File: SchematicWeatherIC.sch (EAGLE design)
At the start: 27 parts, among them U1 ESP32-C6FH4, U2 MIC5365-3.3YC5-TR

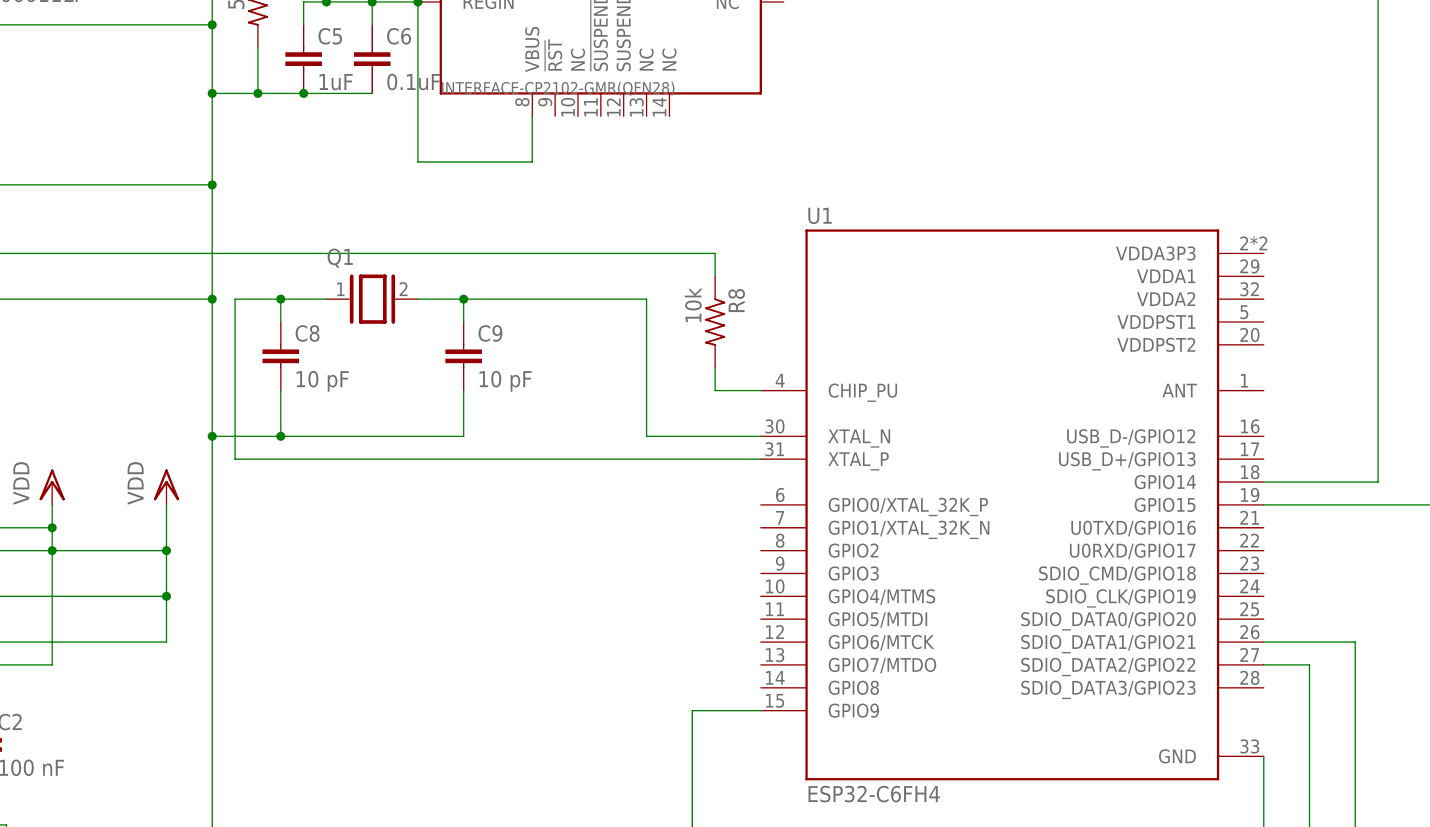
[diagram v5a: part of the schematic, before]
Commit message: connect vdd esp32
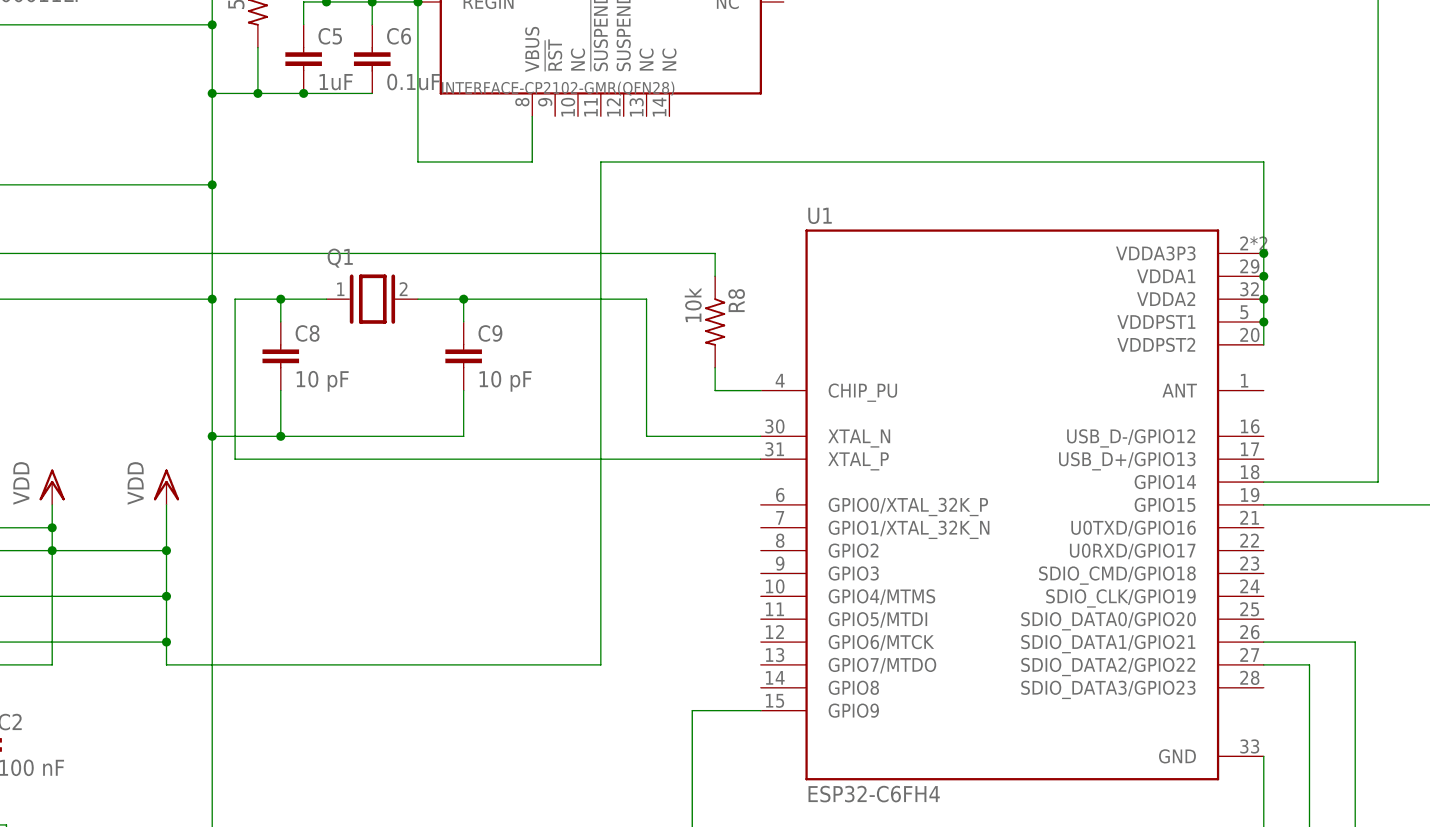
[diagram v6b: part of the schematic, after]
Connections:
- net VDD: now also U1.VDDA1, U1.VDDA2, U1.VDDA3P3, U1.VDDPST1, U1.VDDPST2
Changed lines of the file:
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@@
 <wire x1="58.42" y1="71.12" x2="96.52" y2="71.12" width="0.1524" layer="91"/>
 <junction x="96.52" y="71.12"/>
+<pinref part="U1" gate="G$1" pin="VDDPST2"/>
+<pinref part="U1" gate="G$1" pin="VDDA3P3"/>
+<wire x1="231.14" y1="91.44" x2="231.14" y2="93.98" width="0.1524" layer="91"/>
+<pinref part="U1" gate="G$1" pin="VDDPST1"/>
+<wire x1="231.14" y1="93.98" x2="231.14" y2="96.52" width="0.1524" layer="91"/>
+<junction x="231.14" y="93.98"/>
+<pinref part="U1" gate="G$1" pin="VDDA1"/>
+<wire x1="231.14" y1="96.52" x2="231.14" y2="99.06" width="0.1524" layer="91"/>
+<wire x1="231.14" y1="99.06" x2="231.14" y2="101.6" width="0.1524" layer="91"/>
+<junction x="231.14" y="99.06"/>
+<pinref part="U1" gate="G$1" pin="VDDA2"/>
+<junction x="231.14" y="96.52"/>
+<wire x1="231.14" y1="101.6" x2="231.14" y2="111.76" width="0.1524" layer="91"/>
+<junction x="231.14" y="101.6"/>
+<wire x1="231.14" y1="111.76" x2="157.48" y2="111.76" width="0.1524" layer="91"/>
+<wire x1="157.48" y1="111.76" x2="157.48" y2="55.88" width="0.1524" layer="91"/>
+<wire x1="157.48" y1="55.88" x2="109.22" y2="55.88" width="0.1524" layer="91"/>
+<wire x1="109.22" y1="55.88" x2="109.22" y2="58.42" width="0.1524" layer="91"/>
+<junction x="109.22" y="58.42"/>
 </segment>
 </net>

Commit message: some extra touches
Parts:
- renumbered CP2102 to USBTOSERIAL, Q1 to CRYSTAL, U1 to ESP32, U2 to LDO, USB to USBC

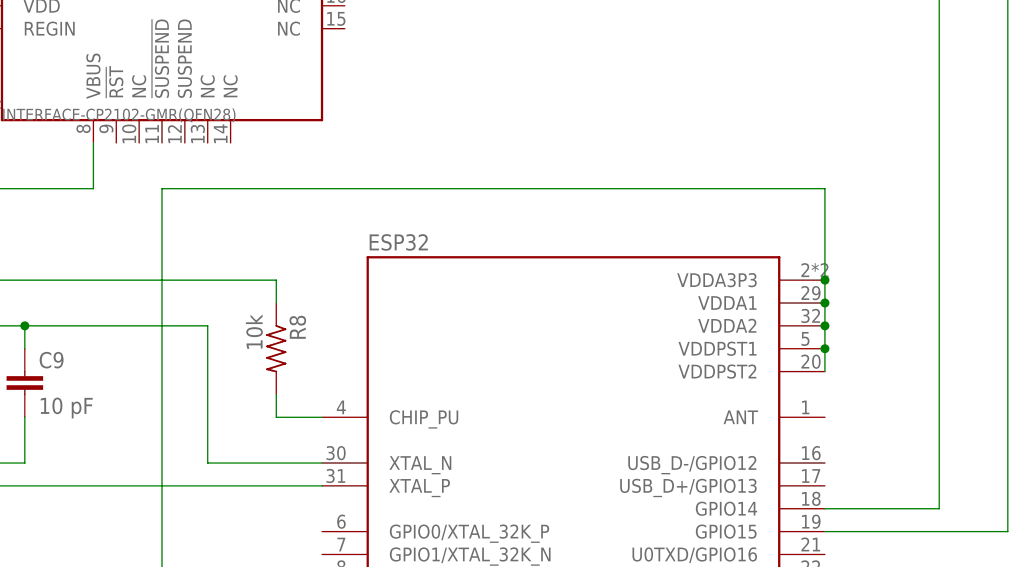
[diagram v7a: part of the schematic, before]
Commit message: add decoupling capacitors to power
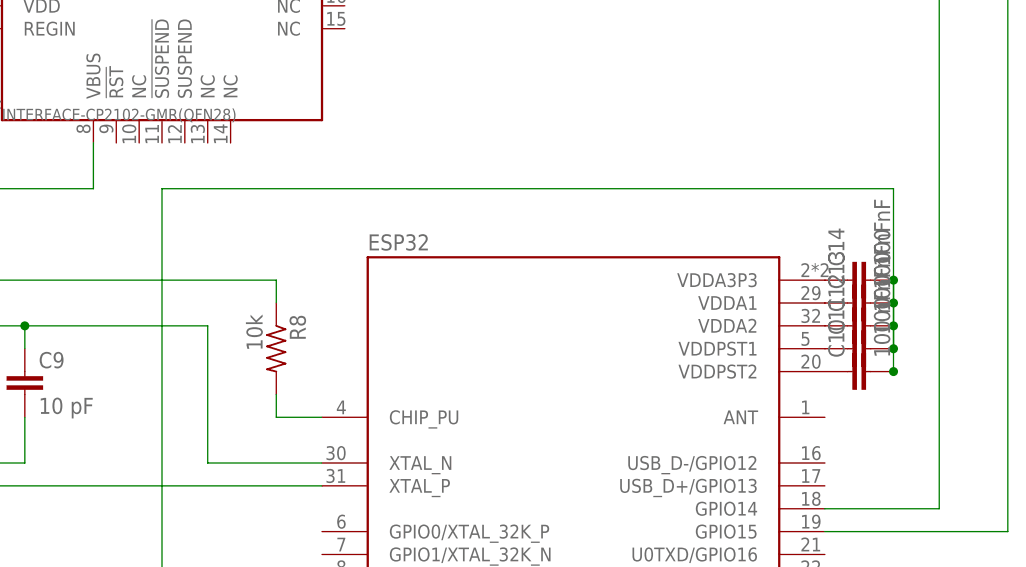
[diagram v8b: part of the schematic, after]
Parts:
- added C10, C11, C12, C13, C14: 100 nF, capacitor-wima:C5/3
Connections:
- new net N$14: C10.1, ESP32.VDDPST2
- new net N$16: C11.1, ESP32.VDDPST1
- new net N$17: C12.1, ESP32.VDDA2
- new net N$18: C13.1, ESP32.VDDA1
- new net N$19: C14.1, ESP32.VDDA3P3
- net VDD: now also C10.2, C11.2, C12.2, C13.2, C14.2; no longer ESP32.VDDA1, ESP32.VDDA2, ESP32.VDDA3P3, ESP32.VDDPST1, ESP32.VDDPST2
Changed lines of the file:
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@@
 <part name="R8" library="rcl" library_urn="urn:adsk.eagle:library:334" deviceset="R-US_" device="VMTB60" package3d_urn="urn:adsk.eagle:package:26122/2" value="10k"/>
 <part name="R9" library="rcl" library_urn="urn:adsk.eagle:library:334" deviceset="R-US_" device="VMTB60" package3d_urn="urn:adsk.eagle:package:26122/2" value="10k"/>
+<part name="C10" library="capacitor-wima" library_urn="urn:adsk.eagle:library:116" deviceset="C" device="5/3" package3d_urn="urn:adsk.eagle:package:5433/1" value="100 nF"/>
+<part name="C11" library="capacitor-wima" library_urn="urn:adsk.eagle:library:116" deviceset="C" device="5/3" package3d_urn="urn:adsk.eagle:package:5433/1" value="100 nF"/>
+<part name="C12" library="capacitor-wima" library_urn="urn:adsk.eagle:library:116" deviceset="C" device="5/3" package3d_urn="urn:adsk.eagle:package:5433/1" value="100 nF"/>
+<part name="C13" library="capacitor-wima" library_urn="urn:adsk.eagle:library:116" deviceset="C" device="5/3" package3d_urn="urn:adsk.eagle:package:5433/1" value="100 nF"/>
+<part name="C14" library="capacitor-wima" library_urn="urn:adsk.eagle:library:116" deviceset="C" device="5/3" package3d_urn="urn:adsk.eagle:package:5433/1" value="100 nF"/>
 </parts>
 <sheets>
@@
 <attribute name="NAME" x="-23.9014" y="92.71" size="1.778" layer="95" rot="R270"/>
 <attribute name="VALUE" x="-28.702" y="92.71" size="1.778" layer="96" rot="R270"/>
+</instance>
+<instance part="C10" gate="G$1" x="233.68" y="91.44" smashed="yes" rot="R90">
+<attribute name="NAME" x="233.299" y="92.964" size="1.778" layer="95" rot="R90"/>
+<attribute name="VALUE" x="238.379" y="92.964" size="1.778" layer="96" rot="R90"/>
+</instance>
+<instance part="C11" gate="G$1" x="233.68" y="93.98" smashed="yes" rot="R90">
+<attribute name="NAME" x="233.299" y="95.504" size="1.778" layer="95" rot="R90"/>
+<attribute name="VALUE" x="238.379" y="95.504" size="1.778" layer="96" rot="R90"/>
+</instance>
+<instance part="C12" gate="G$1" x="233.68" y="96.52" smashed="yes" rot="R90">
+<attribute name="NAME" x="233.299" y="98.044" size="1.778" layer="95" rot="R90"/>
+<attribute name="VALUE" x="238.379" y="98.044" size="1.778" layer="96" rot="R90"/>
+</instance>
+<instance part="C13" gate="G$1" x="233.68" y="99.06" smashed="yes" rot="R90">
+<attribute name="NAME" x="233.299" y="100.584" size="1.778" layer="95" rot="R90"/>
+<attribute name="VALUE" x="238.379" y="100.584" size="1.778" layer="96" rot="R90"/>
+</instance>
+<instance part="C14" gate="G$1" x="233.68" y="101.6" smashed="yes" rot="R90">
+<attribute name="NAME" x="233.299" y="103.124" size="1.778" layer="95" rot="R90"/>
+<attribute name="VALUE" x="238.379" y="103.124" size="1.778" layer="96" rot="R90"/>
 </instance>
 </instances>
@@
 <wire x1="58.42" y1="71.12" x2="96.52" y2="71.12" width="0.1524" layer="91"/>
 <junction x="96.52" y="71.12"/>
-<pinref part="ESP32" gate="G$1" pin="VDDPST2"/>
-<pinref part="ESP32" gate="G$1" pin="VDDA3P3"/>
-<wire x1="231.14" y1="91.44" x2="231.14" y2="93.98" width="0.1524" layer="91"/>
-<pinref part="ESP32" gate="G$1" pin="VDDPST1"/>
-<wire x1="231.14" y1="93.98" x2="231.14" y2="96.52" width="0.1524" layer="91"/>
-<junction x="231.14" y="93.98"/>
-<pinref part="ESP32" gate="G$1" pin="VDDA1"/>
-<wire x1="231.14" y1="96.52" x2="231.14" y2="99.06" width="0.1524" layer="91"/>
-<wire x1="231.14" y1="99.06" x2="231.14" y2="101.6" width="0.1524" layer="91"/>
-<junction x="231.14" y="99.06"/>
-<pinref part="ESP32" gate="G$1" pin="VDDA2"/>
-<junction x="231.14" y="96.52"/>
-<wire x1="231.14" y1="101.6" x2="231.14" y2="111.76" width="0.1524" layer="91"/>
-<junction x="231.14" y="101.6"/>
-<wire x1="231.14" y1="111.76" x2="157.48" y2="111.76" width="0.1524" layer="91"/>
+<wire x1="238.76" y1="111.76" x2="157.48" y2="111.76" width="0.1524" layer="91"/>
 <wire x1="157.48" y1="111.76" x2="157.48" y2="55.88" width="0.1524" layer="91"/>
 <wire x1="157.48" y1="55.88" x2="109.22" y2="55.88" width="0.1524" layer="91"/>
 <wire x1="109.22" y1="55.88" x2="109.22" y2="58.42" width="0.1524" layer="91"/>
 <junction x="109.22" y="58.42"/>
+<pinref part="C10" gate="G$1" pin="2"/>
+<pinref part="C11" gate="G$1" pin="2"/>
+<wire x1="238.76" y1="93.98" x2="238.76" y2="96.52" width="0.1524" layer="91"/>
+<junction x="238.76" y="93.98"/>
+<pinref part="C12" gate="G$1" pin="2"/>
+<wire x1="238.76" y1="96.52" x2="238.76" y2="99.06" width="0.1524" layer="91"/>
+<junction x="238.76" y="96.52"/>
+<pinref part="C13" gate="G$1" pin="2"/>
+<wire x1="238.76" y1="99.06" x2="238.76" y2="101.6" width="0.1524" layer="91"/>
+<junction x="238.76" y="99.06"/>
+<pinref part="C14" gate="G$1" pin="2"/>
+<wire x1="238.76" y1="101.6" x2="238.76" y2="111.76" width="0.1524" layer="91"/>
+<junction x="238.76" y="101.6"/>
+<wire x1="238.76" y1="101.6" x2="238.76" y2="93.98" width="0.1524" layer="91"/>
+<junction x="238.76" y="91.44"/>
+<wire x1="238.76" y1="91.44" x2="238.76" y2="93.98" width="0.1524" layer="91"/>
 </segment>
 </net>
@@
 </segment>
 </net>
+<net name="N$14" class="0">
+<segment>
+<pinref part="ESP32" gate="G$1" pin="VDDPST2"/>
+<pinref part="C10" gate="G$1" pin="1"/>
+</segment>
+</net>
+<net name="N$16" class="0">
+<segment>
+<pinref part="ESP32" gate="G$1" pin="VDDPST1"/>
+<pinref part="C11" gate="G$1" pin="1"/>
+</segment>
+</net>
+<net name="N$17" class="0">
+<segment>
+<pinref part="ESP32" gate="G$1" pin="VDDA2"/>
+<pinref part="C12" gate="G$1" pin="1"/>
+</segment>
+</net>
+<net name="N$18" class="0">
+<segment>
+<pinref part="ESP32" gate="G$1" pin="VDDA1"/>
+<pinref part="C13" gate="G$1" pin="1"/>
+</segment>
+</net>
+<net name="N$19" class="0">
+<segment>
+<pinref part="ESP32" gate="G$1" pin="VDDA3P3"/>
+<pinref part="C14" gate="G$1" pin="1"/>
+</segment>
+</net>
